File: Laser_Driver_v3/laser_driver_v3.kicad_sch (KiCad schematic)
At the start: 0 parts

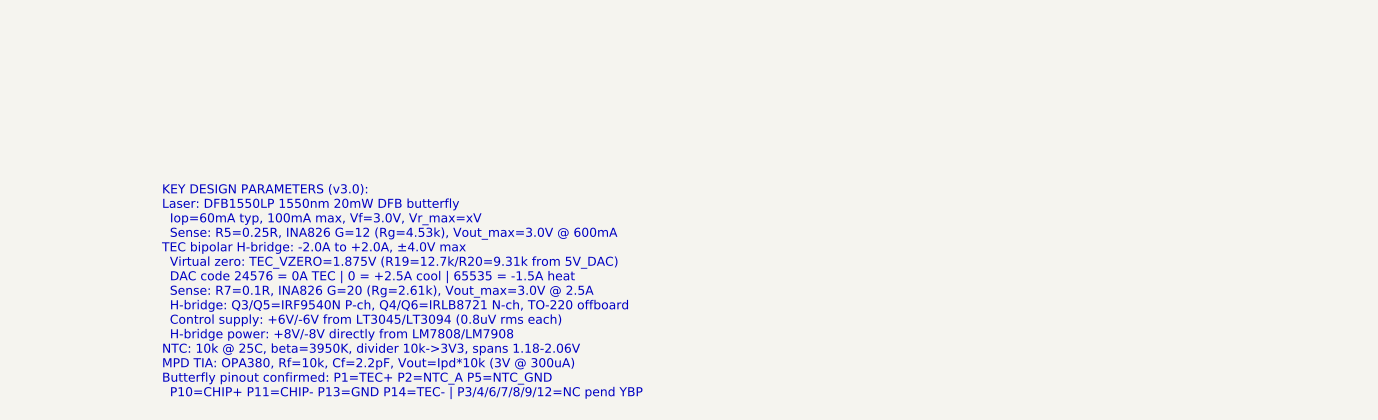
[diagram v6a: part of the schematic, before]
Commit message: 6 V supply. Annotations. Teensy zero current.
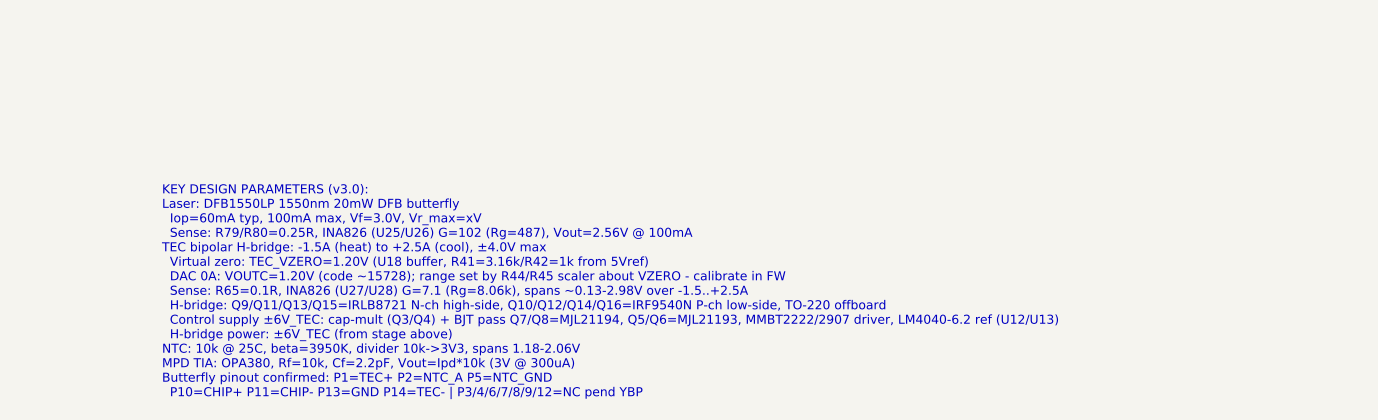
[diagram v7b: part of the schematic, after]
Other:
- note added: "KEY DESIGN PARAMETERS (v3.0): Laser: DFB1550LP 1550nm 20mW DFB butterfly Iop=60mA typ, 100mA max, Vf=3.0V, Vr_max=xV Sense: R79/R80=0.25R, INA826 (U25/U26) G=102 (Rg=487), Vout=2.56V @ 100mA TEC bipolar H-bridge: -1.5A (heat) to +2.5A (cool), ±4.0V max Virtual zero: TEC_VZERO=1.20V (U18 buffer, R41=3.16k/R42=1k from 5Vref) DAC 0A: VOUTC=1.20V (code ~15728); range set by R44/R45 scaler about VZERO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"
- note removed: "KEY DESIGN PARAMETERS (v3.0): Laser: DFB1550LP 1550nm 20mW DFB butterfly Iop=60mA typ, 100mA max, Vf=3.0V, Vr_max=xV Sense: R5=0.25R, INA826 G=12 (Rg=4.53k), Vout_max=3.0V @ 600mA TEC bipolar H-bridge: -2.0A to +2.0A, ±4.0V max Virtual zero: TEC_VZERO=1.875V (R19=12.7k/R20=9.31k from 5V_DAC) DAC code 24576 = 0A TEC | 0 = +2.5A cool | 65535 = -1.5A heat Sense: R7=0.1R, INA826 G=20 (Rg=2.61k), Vout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"
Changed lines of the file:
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@@
 		(rev "3.0")
 		(company "Stefan Cular")
-		(comment 1 "1550nm 70mW DFB butterfly | Bipolar TEC H-bridge -1.5A/+2.5A | AD5064 16-bit DAC")
+		(comment 1 "1550nm 20mW DFB butterfly | Bipolar TEC H-bridge -1.5A/+2.5A | AD5064 16-bit DAC")
 		(comment 2 "Rail2: LM7807->LT3042->LTC6655-5 | Rail3: LM7805->RC->LT3045 | Rail4/5: ±LM780x->LT3045/94")
 		(comment 3 "Readback: INA826 laser+TEC current, NTC thermistor divider, OPA380 MPD TIA")
@@
 		)
 	)
-	(text "KEY DESIGN PARAMETERS (v3.0):\nLaser: DFB1550LP 1550nm 20mW DFB butterfly\n  Iop=60mA typ, 100mA max, Vf=3.0V, Vr_max=xV\n  Sense: R5=0.25R, INA826 G=12 (Rg=4.53k), Vout_max=3.0V @ 600mA\nTEC bipolar H-bridge: -2.0A to +2.0A, ±4.0V max\n  Virtual zero: TEC_VZERO=1.875V (R19=12.7k/R20=9.31k from 5V_DAC)\n  DAC code 24576 = 0A TEC | 0 = +2.5A cool | 65535 = -1.5A heat\n  Sense: R7=0.1R, INA826 G=20 (Rg=2.61k), Vout_max=3.0V @ 2.5A\n  H-bridge: Q3/Q5=IRF9540N P-ch, Q4/Q6=IRLB8721 N-ch, TO-220 offboard\n  Control supply: +6V/-6V from LT3045/LT3094 (0.8uV rms each)\n  H-bridge power: +8V/-8V directly from LM7808/LM7908\nNTC: 10k @ 25C, beta=3950K, divider 10k->3V3, spans 1.18-2.06V\nMPD TIA: OPA380, Rf=10k, Cf=2.2pF, Vout=Ipd*10k (3V @ 300uA)\nButterfly pinout confirmed: P1=TEC+ P2=NTC_A P5=NTC_GND\n  P10=CHIP+ P11=CHIP- P13=GND P14=TEC- | P3/4/6/7/8/9/12=NC pend YBP"
+	(text "KEY DESIGN PARAMETERS (v3.0):\nLaser: DFB1550LP 1550nm 20mW DFB butterfly\n  Iop=60mA typ, 100mA max, Vf=3.0V, Vr_max=xV\n  Sense: R79/R80=0.25R, INA826 (U25/U26) G=102 (Rg=487), Vout=2.56V @ 100mA\nTEC bipolar H-bridge: -1.5A (heat) to +2.5A (cool), ±4.0V max\n  Virtual zero: TEC_VZERO=1.20V (U18 buffer, R41=3.16k/R42=1k from 5Vref)\n  DAC 0A: VOUTC=1.20V (code ~15728); range set by R44/R45 scaler about VZERO - calibrate in FW\n  Sense: R65=0.1R, INA826 (U27/U28) G=7.1 (Rg=8.06k), spans ~0.13-2.98V over -1.5..+2.5A\n  H-bridge: Q9/Q11/Q13/Q15=IRLB8721 N-ch high-side, Q10/Q12/Q14/Q16=IRF9540N P-ch low-side, TO-220 offboard\n  Control supply ±6V_TEC: cap-mult (Q3/Q4) + BJT pass Q7/Q8=MJL21194, Q5/Q6=MJL21193, MMBT2222/2907 driver, LM4040-6.2 ref (U12/U13)\n  H-bridge power: ±6V_TEC (from stage above)\nNTC: 10k @ 25C, beta=3950K, divider 10k->3V3, spans 1.18-2.06V\nMPD TIA: OPA380, Rf=10k, Cf=2.2pF, Vout=Ipd*10k (3V @ 300uA)\nButterfly pinout confirmed: P1=TEC+ P2=NTC_A P5=NTC_GND\n  P10=CHIP+ P11=CHIP- P13=GND P14=TEC- | P3/4/6/7/8/9/12=NC pend YBP"
 		(exclude_from_sim no)
 		(at 201.676 145.034 0)

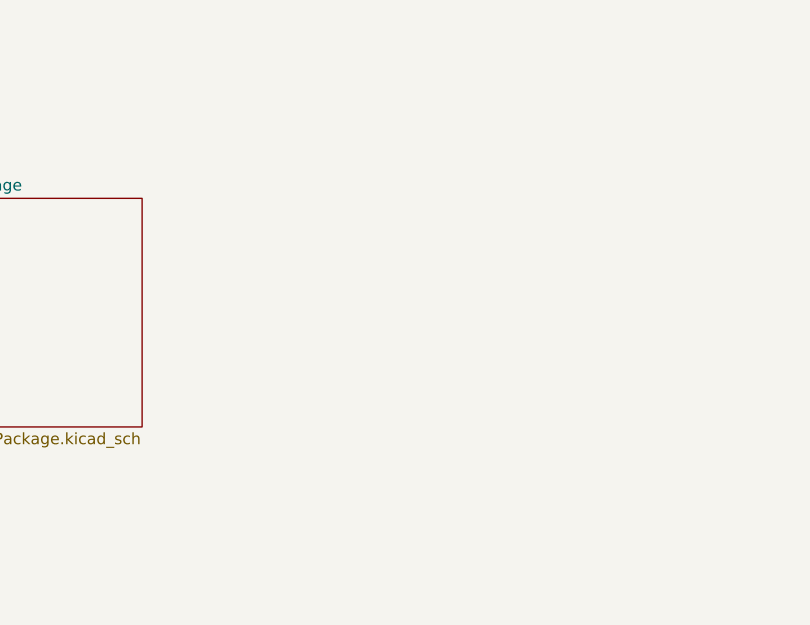
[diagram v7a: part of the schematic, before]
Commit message: Changed to an RF modulation
Based on the uncertainty calculation, needed to change from a low frequency modulation to an RF modulation.  This drive down the noise, but required a very different implentation.  The modulation is limited to about 2 MHz.  Much faster is at the limit of this hardware and would require significant increase in complexity and cost.
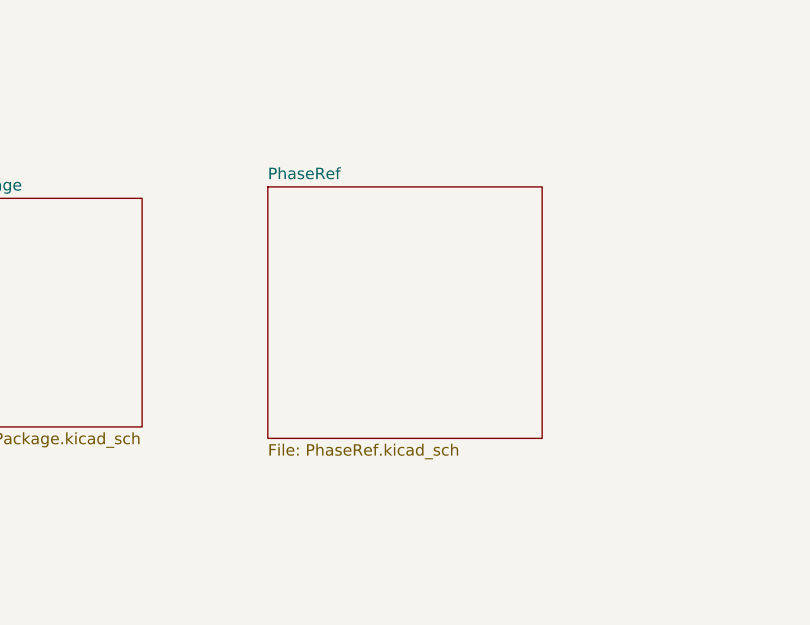
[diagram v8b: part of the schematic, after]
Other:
- added sheet PhaseRef (PhaseRef.kicad_sch)
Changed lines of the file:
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@@
+	)
+	(sheet
+		(at 182.88 66.04)
+		(size 30.48 27.94)
+		(exclude_from_sim no)
+		(in_bom yes)
+		(on_board yes)
+		(dnp no)
+		(fields_autoplaced yes)
+		(stroke
+			(width 0.1524)
+			(type solid)
+		)
+		(fill
+			(color 0 0 0 0)
+		)
+		(property "Sheetname" "PhaseRef"
+			(at 182.88 65.3284 0)
+			(show_name no)
+			(do_not_autoplace no)
+			(effects
+				(font
+					(size 1.27 1.27)
+				)
+				(justify left bottom)
+			)
+		)
+		(property "Sheetfile" "PhaseRef.kicad_sch"
+			(at 182.88 94.5646 0)
+			(show_name no)
+			(do_not_autoplace no)
+			(effects
+				(font
+					(size 1.27 1.27)
+				)
+				(justify left top)
+			)
+		)
+		(instances
+			(project "laser_driver_v3"
+				(path "/b2c3d4e5-f6a7-8901-bcde-f12345678901"
+					(page "15")
+				)
+			)
+		)
 	)
 	(sheet
